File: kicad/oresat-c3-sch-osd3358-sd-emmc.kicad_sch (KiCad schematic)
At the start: 65 parts, among them J5 DM3BT-DSF-PEJS, U1 OSD3358-512M-BSM, U8 TCAN330, U9 EMMC+RESET+5.1-COMPATIBLE-BA

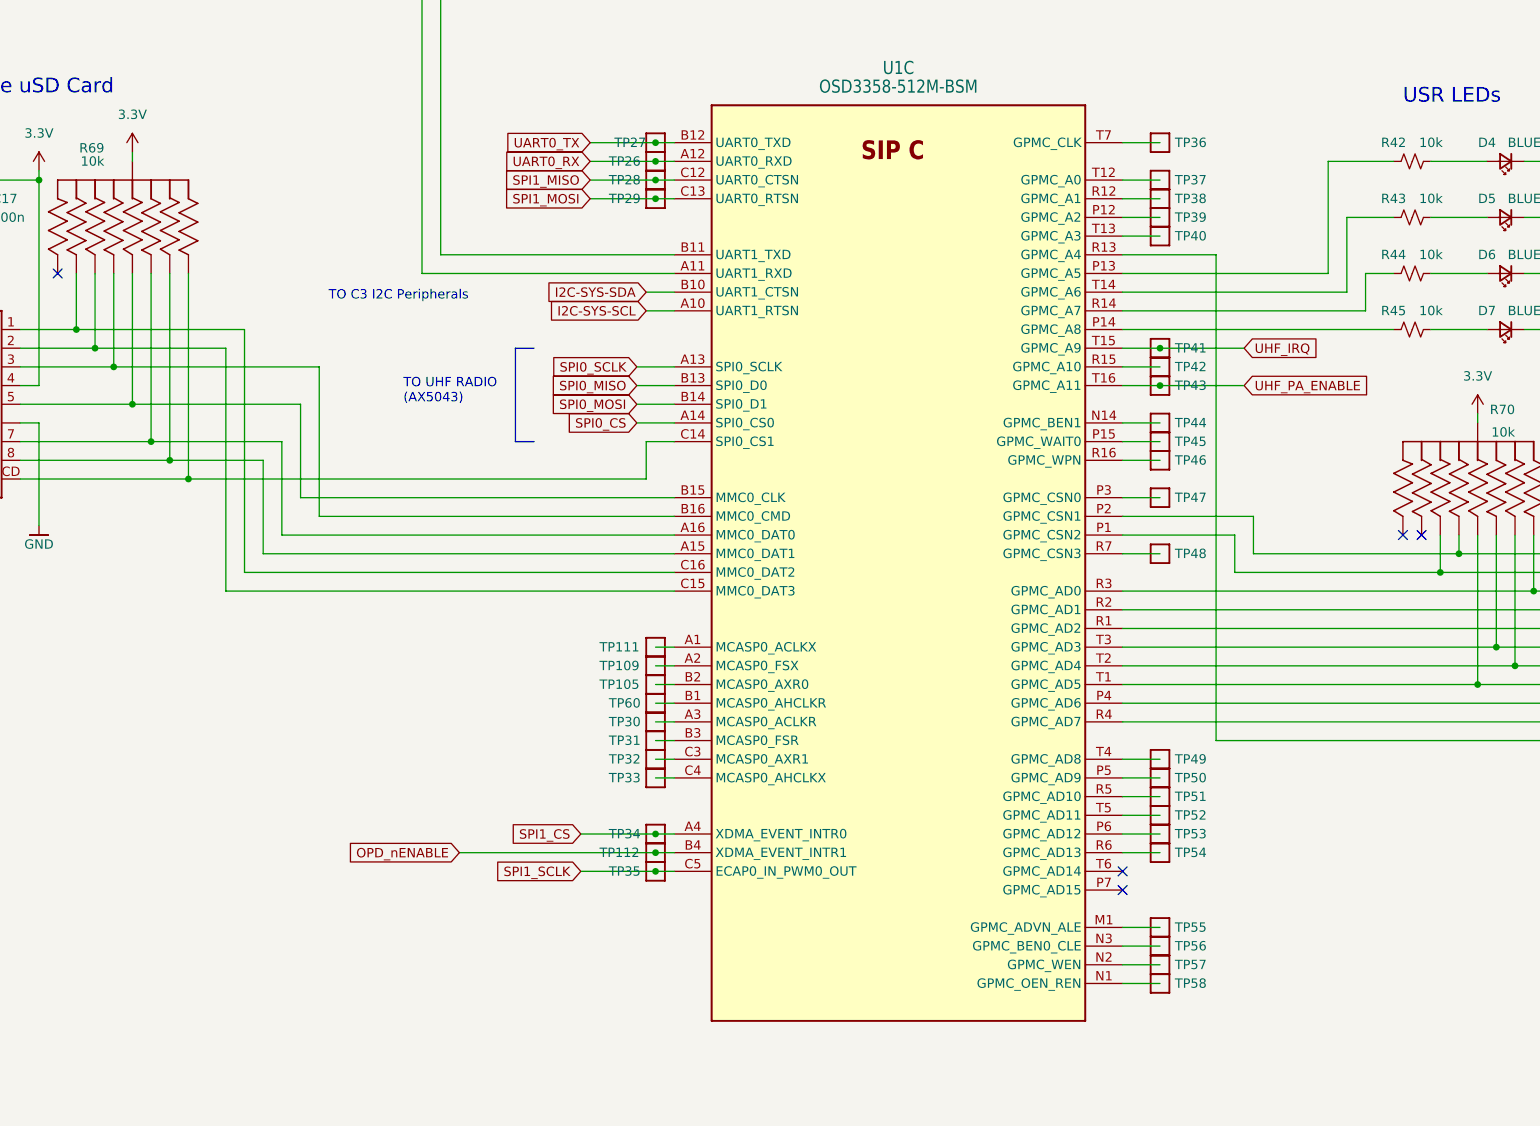
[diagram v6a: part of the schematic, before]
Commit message: Big C3 cleanup with Glenn; radios off of one SPS + separate LDOs, removed lots of test 0 ohm resistors, cleaned up capacitance, and finally wired everything up to the octavo. ZERO ERC errors.
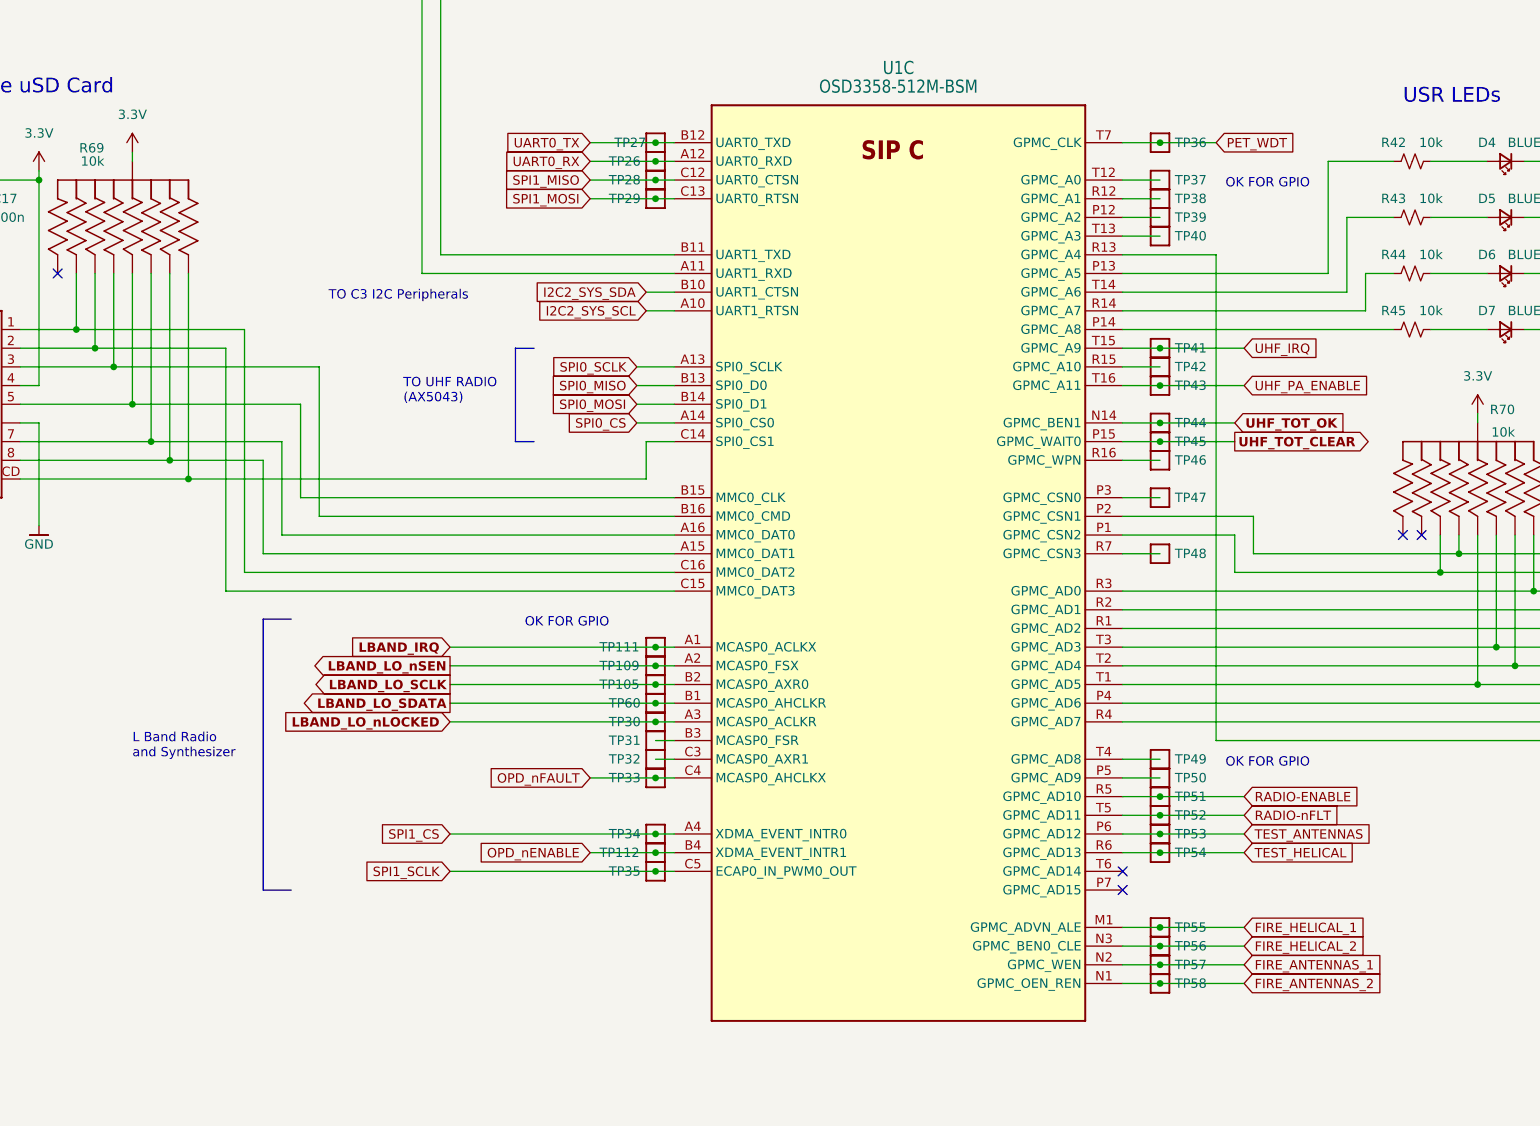
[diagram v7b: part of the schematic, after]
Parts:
- TP105, TP109, TP111, TP112, TP23, TP24, TP26, TP27, TP28, TP29, TP30, TP31, TP32, TP33, TP34, TP35, TP36, TP37, TP38, TP39, TP40, TP41, TP42, TP43, TP44, TP45, TP46, TP47, TP48, TP49, TP50, TP51, TP52, TP53, TP54, TP55, TP56, TP57, TP58, TP60: footprint oresat-misc:PAD.03X.04 -> TestPoint:TestPoint_Pad_D1.0mm; symbol oresat-misc:Test-Point -> oresat-misc:Test-Point-1mm-round
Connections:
- net OPD_nFAULT: now reaches TP33.1, U1.C4 (MCASP0_AHCLKX)
- net FIRE_HELICAL_1: now reaches TP55.1, U1.M1 (GPMC_ADVN_ALE)
- net FIRE_ANTENNAS_2: now reaches TP58.1, U1.N1 (GPMC_OEN_REN)
- net RADIO-ENABLE: now reaches TP51.1, U1.R5 (GPMC_AD10)
- net UHF_TOT_CLEAR: now reaches TP45.1, U1.P15 (GPMC_WAIT0)
- net LBAND_IRQ: now reaches TP111.1, U1.A1 (MCASP0_ACLKX)
- net RADIO-nFLT: now reaches TP52.1, U1.T5 (GPMC_AD11)
- net LBAND_LO_nSEN: now reaches TP109.1, U1.A2 (MCASP0_FSX)
- net LBAND_LO_nLOCKED: now reaches TP30.1, U1.A3 (MCASP0_ACLKR)
- net LBAND_LO_SDATA: now reaches TP60.1, U1.B1 (MCASP0_AHCLKR)
- net LBAND_LO_SCLK: now reaches TP105.1, U1.B2 (MCASP0_AXR0)
- net UHF_TOT_OK: now reaches TP44.1, U1.N14 (GPMC_BEN1)
- net FIRE_ANTENNAS_1: now reaches TP57.1, U1.N2 (GPMC_WEN)
- net FIRE_HELICAL_2: now reaches TP56.1, U1.N3 (GPMC_BEN0_CLE)
- net TEST_ANTENNAS: now reaches TP53.1, U1.P6 (GPMC_AD12)
- net TEST_HELICAL: now reaches TP54.1, U1.R6 (GPMC_AD13)
- net PET_WDT: now reaches TP36.1, U1.T7 (GPMC_CLK)
- net I2C-SYS-SCL renamed I2C2_SYS_SCL
- net I2C-SYS-SDA renamed I2C2_SYS_SDA
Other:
- note added: "L Band Radio and Synthesizer"
- note added: "OK FOR GPIO"

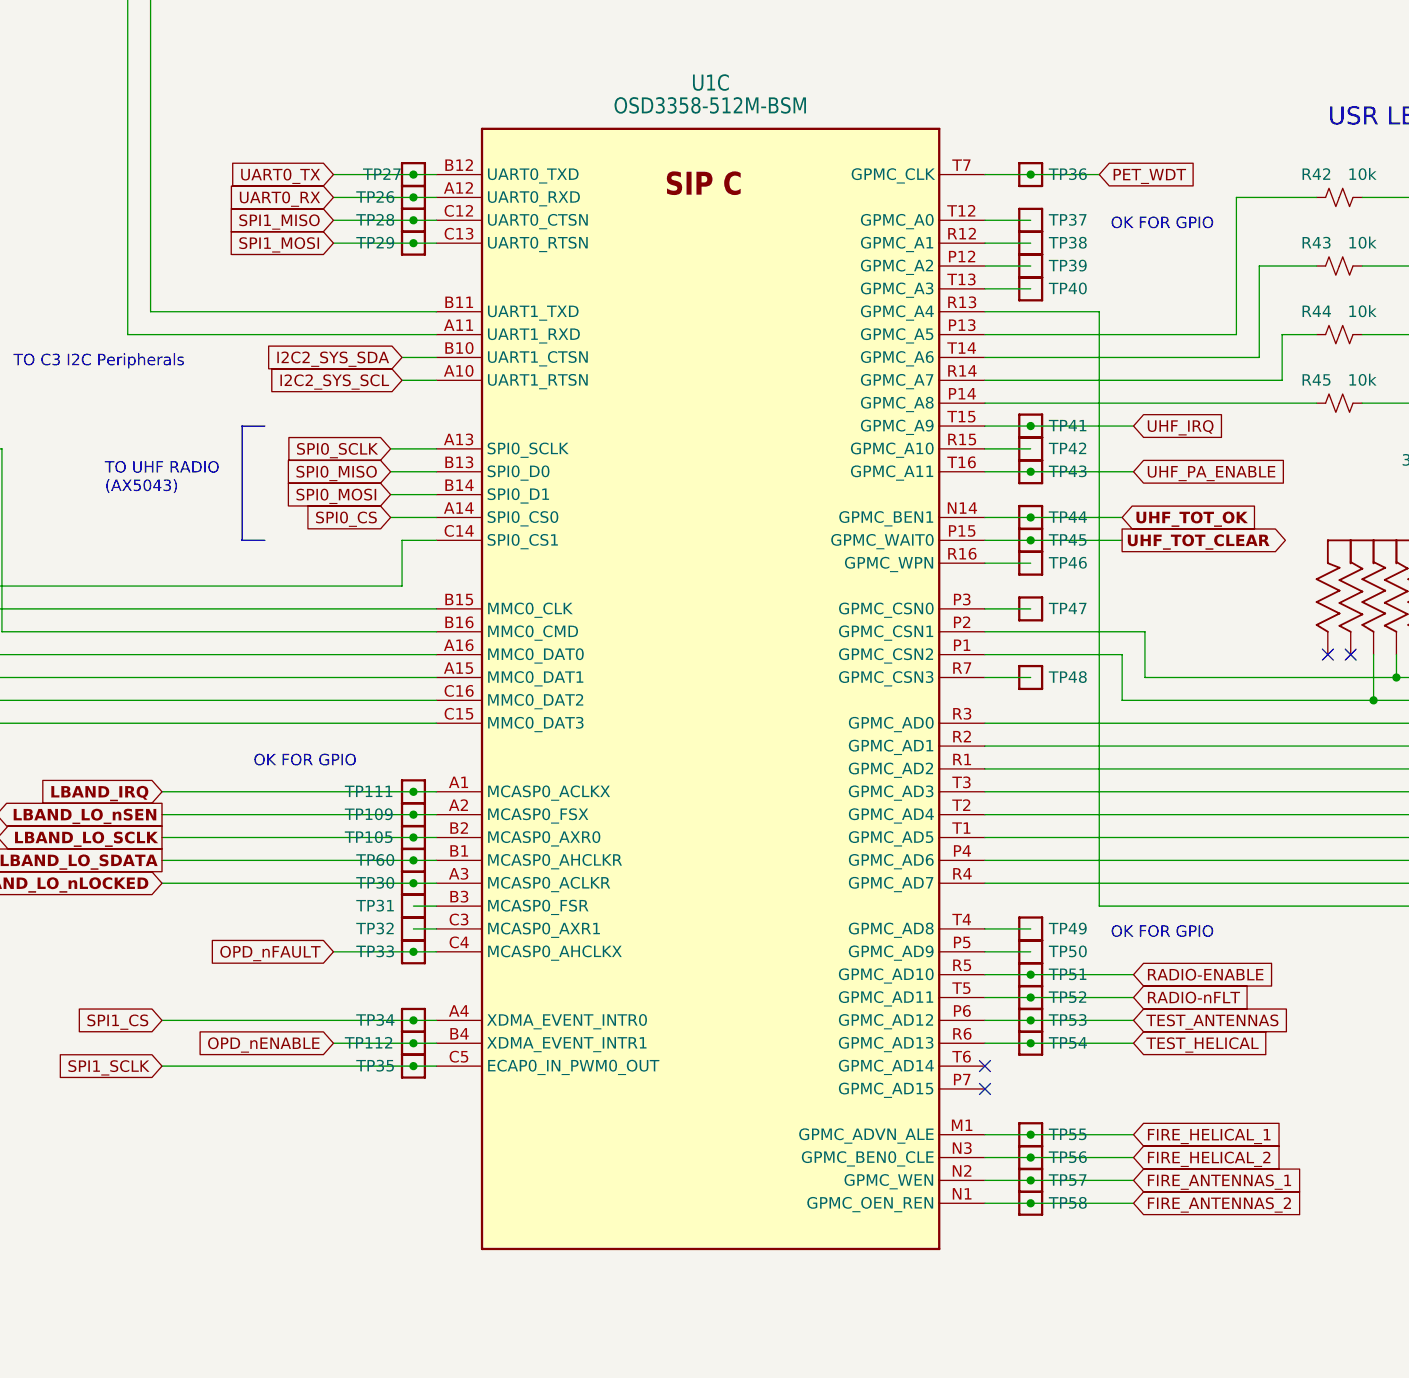
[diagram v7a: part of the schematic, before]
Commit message: Updated test points, fixed some more hidden ERCs.
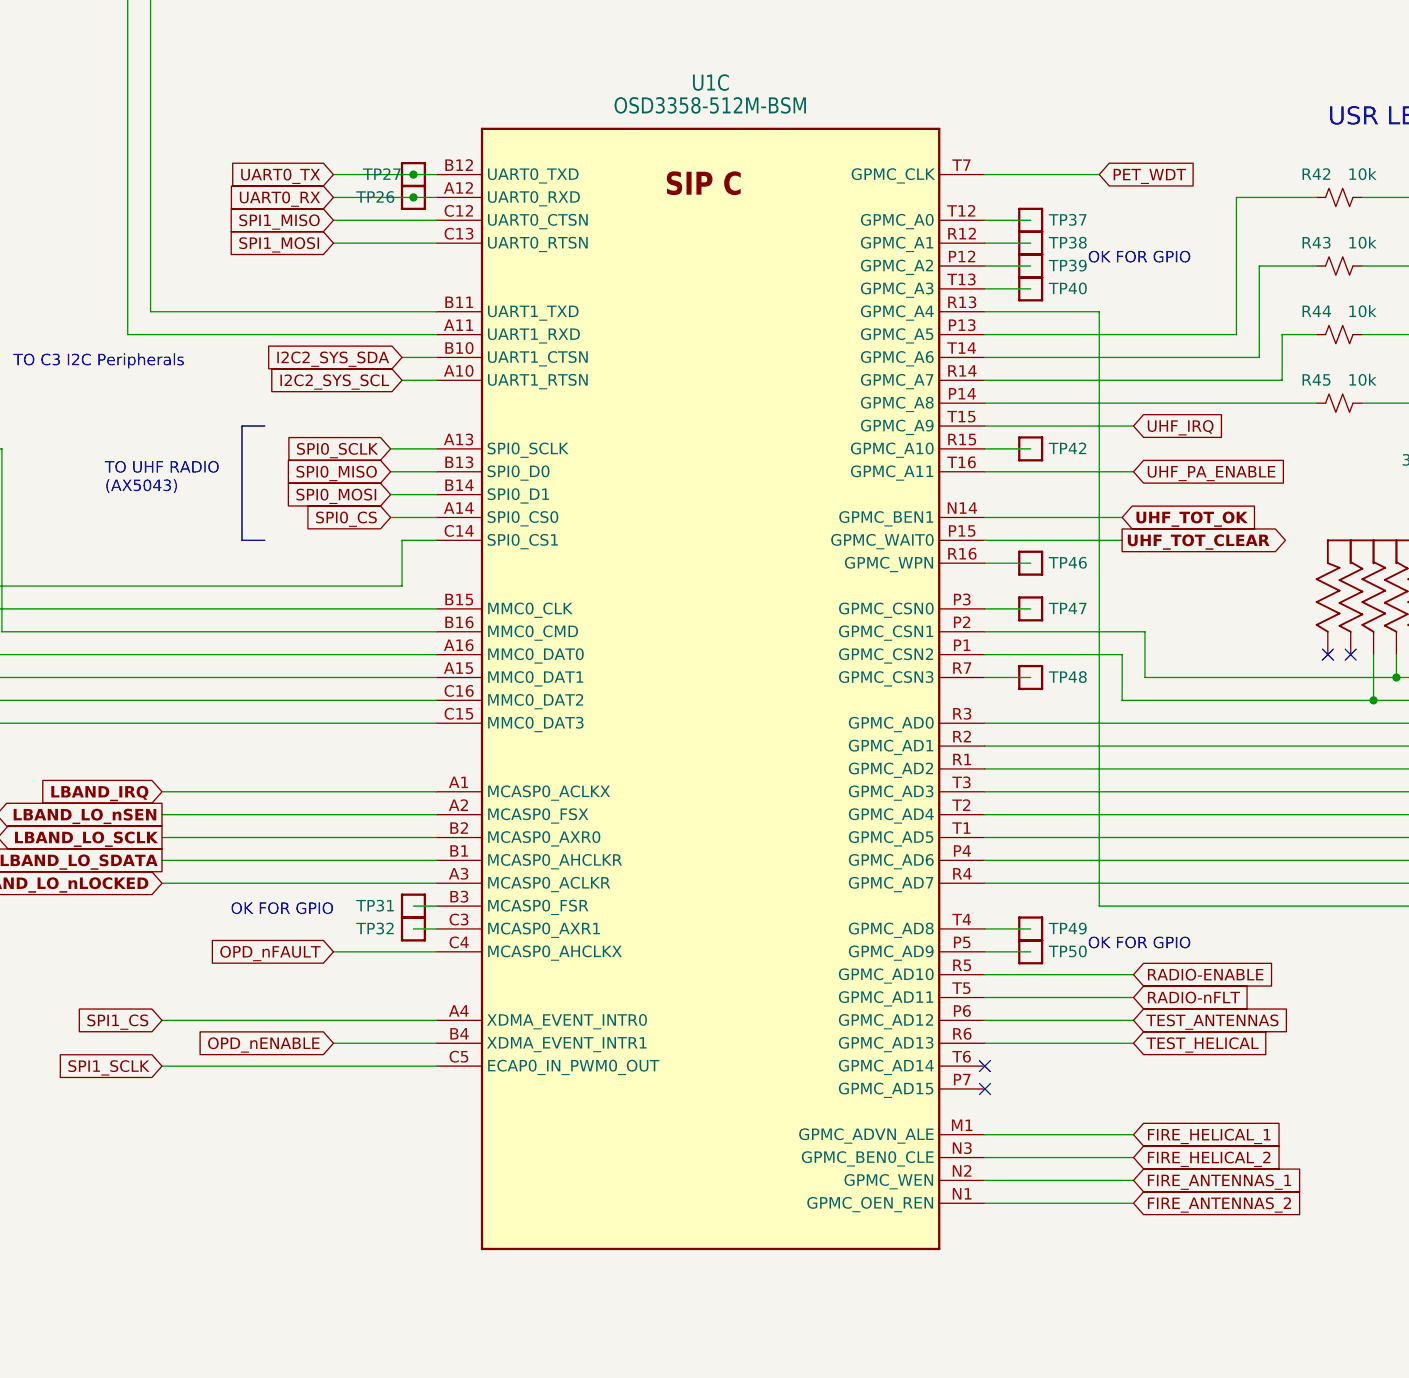
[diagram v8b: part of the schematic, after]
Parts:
- removed TP105, TP109, TP111, TP112, TP28, TP29, TP30, TP33, TP34, TP35, TP36, TP41, TP43, TP44, TP45, TP51, TP52, TP53, TP54, TP55, TP56, TP57, TP58, TP60: Test-Point, TestPoint:TestPoint_Pad_D1.0mm, symbol oresat-misc:Test-Point-1mm-round
